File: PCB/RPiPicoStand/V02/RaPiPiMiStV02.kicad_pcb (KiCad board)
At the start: 4 copper layers, 55.5 x 73 mm, 27 parts, among them U1-PICO W Pico

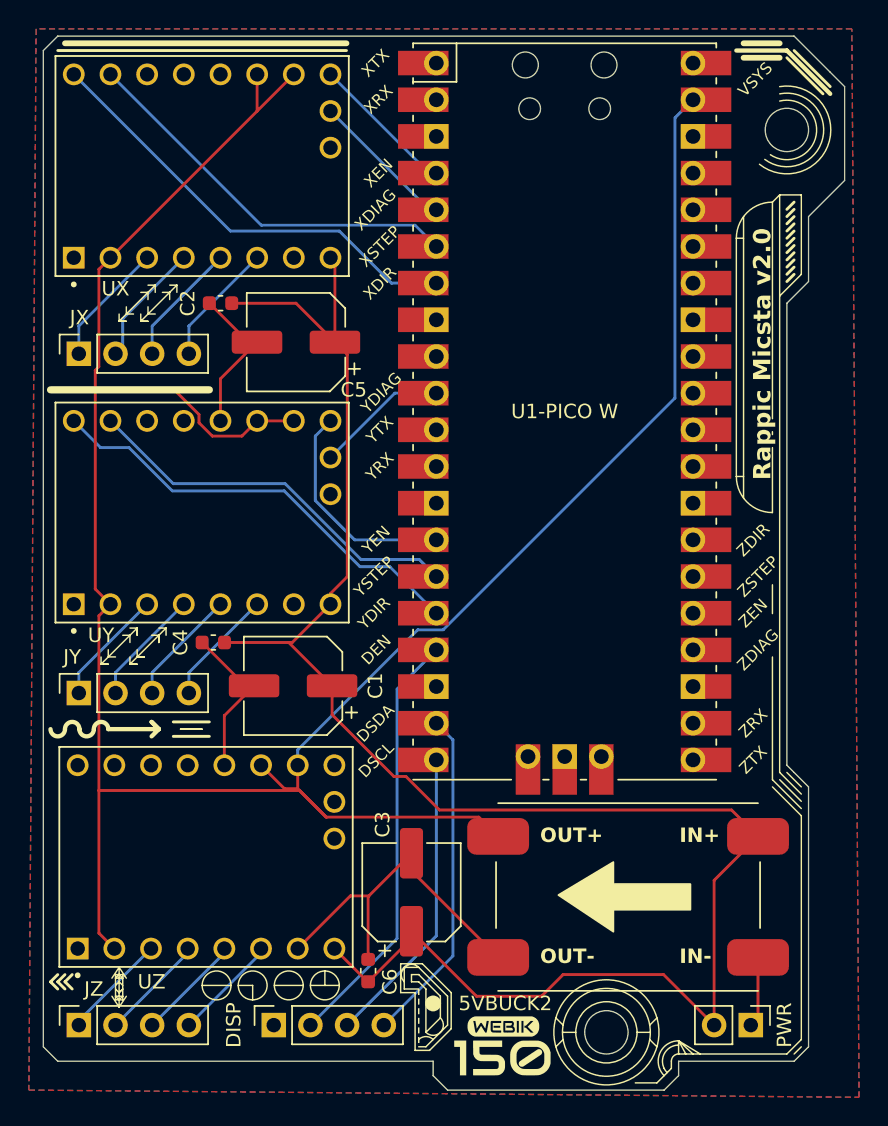
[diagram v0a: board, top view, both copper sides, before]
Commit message: fix uart connections on the PCB
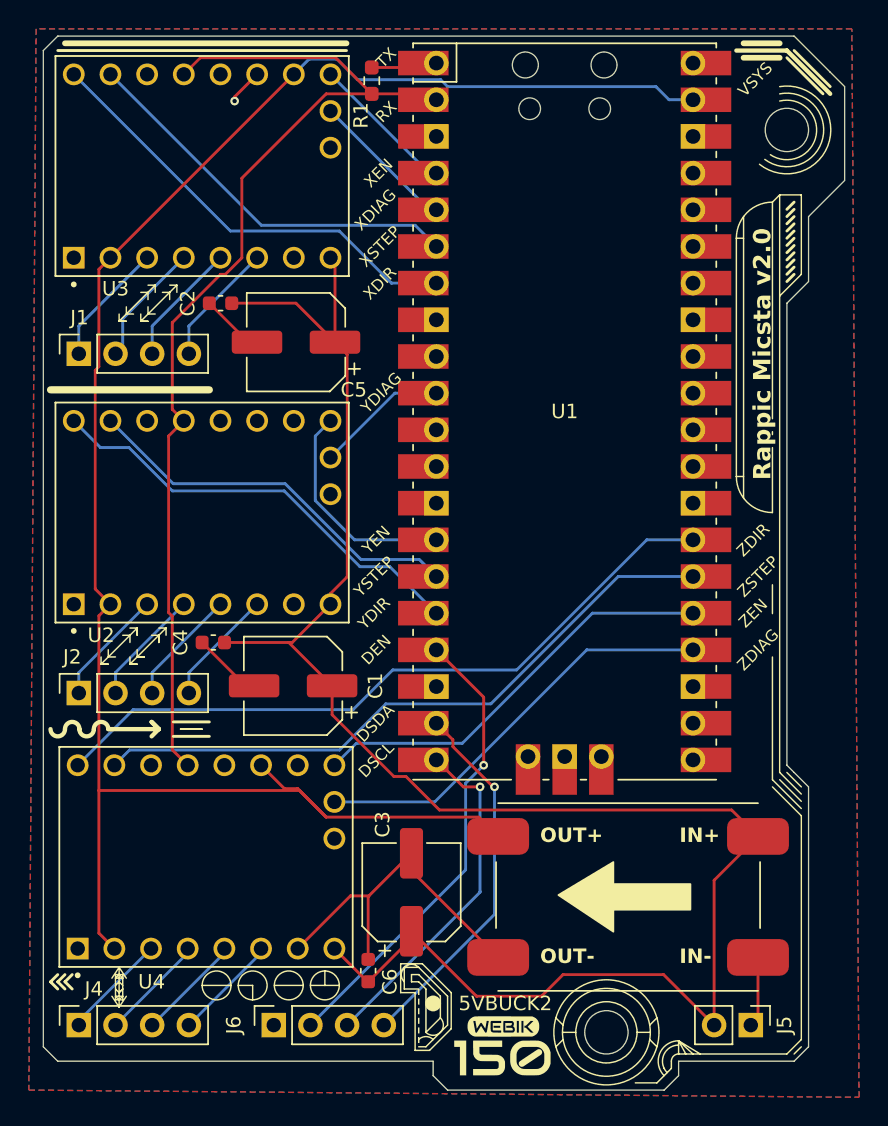
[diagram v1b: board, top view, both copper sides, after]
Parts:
- added R1: R_Small, Resistor_SMD:R_0603_1608Metric_Pad0.98x0.95mm_HandSolder, F.Cu at (170.2, 53.1)
- U1: renamed from U1-PICO W
- renumbered JX to J1, JY to J2, JZ to J4, PWR to J5, DISP to J6, UY to U2, UX to U3, UZ to U4
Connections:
- U1 pad 11: Net-(U1-GPIO8) -> unconnected-(U1-GPIO8-Pad11)
- U1 pad 12: Net-(U1-GPIO8) -> unconnected-(U1-GPIO9-Pad12)_1
- U1 pad 2: Net-(U1-GPIO0) -> Net-(U1-GPIO1)
- U1 pad 21: Net-(U1-GPIO16) -> unconnected-(U1-GPIO16-Pad21)
- U1 pad 22: Net-(U1-GPIO16) -> unconnected-(U1-GPIO17-Pad22)_1
- U2 pad 11: GND -> unconnected-(U2-PDN-Pad11)
- U2 pad 12: Net-(U1-GPIO8) -> Net-(U1-GPIO1)
- U2 pad 13: GND -> unconnected-(U2-SPRD-Pad13)
- U2 pad 14: Net-(5VBUCK2-OUT+) -> GND
- U2 pad 15: Net-(5VBUCK2-OUT+) -> GND
- U3 pad 11: GND -> unconnected-(U3-PDN-Pad11)
- U3 pad 12: Net-(U1-GPIO0) -> Net-(U1-GPIO1)
- U3 pad 13: GND -> unconnected-(U3-SPRD-Pad13)
- U3 pad 14: Net-(5VBUCK2-OUT+) -> GND
- U4 pad 11: GND -> unconnected-(U4-PDN-Pad11)
- U4 pad 12: Net-(U1-GPIO16) -> Net-(U1-GPIO1)
- U4 pad 13: GND -> unconnected-(U4-SPRD-Pad13)
- U4 pad 15: Net-(5VBUCK2-OUT+) -> GND
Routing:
- net Net-(U1-GPIO1): track 0.00 -> 74.8 mm
- net Net-(5VBUCK2-OUT+): track 180.9 -> 131.7 mm
- net Net-(U1-GPIO16): track 46.2 -> 0.00 mm
- net Net-(U1-GPIO8): track 24.7 -> 0.00 mm
- net Net-(U1-GPIO0): track 20.8 -> 4.60 mm
- net GND: track 51.7 -> 41.4 mm, vias 0 -> 1
- net Net-(J6-Pin_3): track 20.9 -> 24.1 mm, vias 0 -> 1
- net Net-(J6-Pin_2): track 29.6 -> 32.3 mm, vias 0 -> 1
- net Net-(J6-Pin_4): track 23.4 -> 25.8 mm, vias 0 -> 1
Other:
- copper layers 4 -> 2

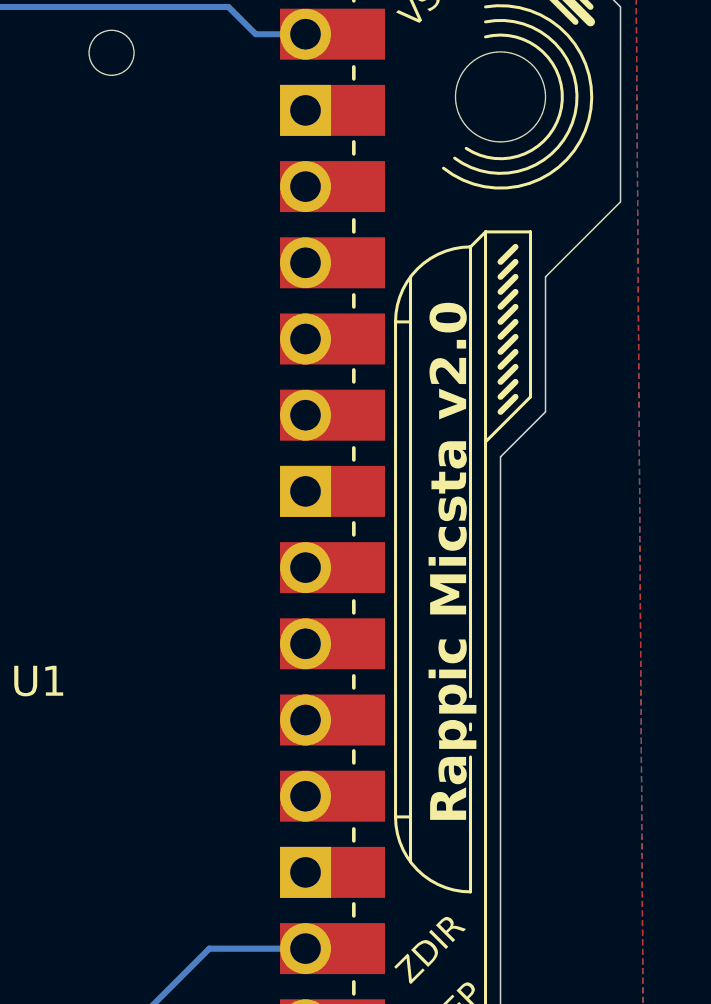
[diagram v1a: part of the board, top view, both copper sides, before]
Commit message: Update PCB design to V2.1 and adjust related files
Updated the PCB to version 2.1, introducing a simpler and cheaper 2-layer design compatible with more TMC2209 types. Adjusted KiCad project settings, output directories, and port configurations to align with the new PCB version. Updated README to document the changes.
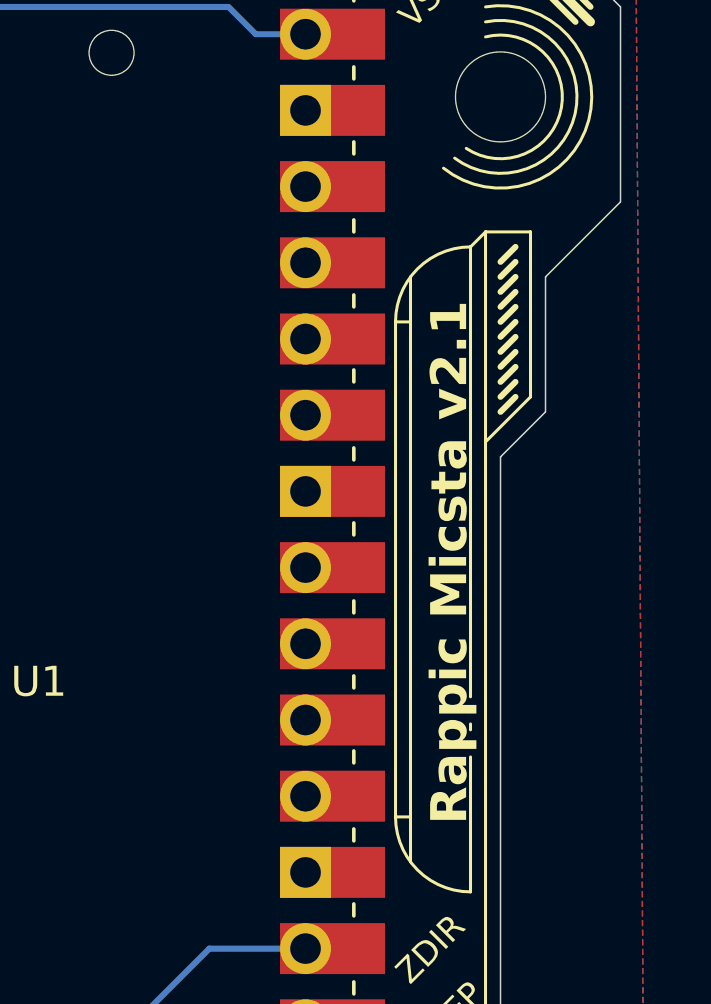
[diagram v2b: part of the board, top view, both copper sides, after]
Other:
- board text added: "Rappic Micsta v2.1"
- board text removed: "Rappic Micsta v2.0"
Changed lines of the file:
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@@
 			(drillshape 0)
 			(scaleselection 1)
-			(outputdirectory "")
+			(outputdirectory "factory-output/v21/")
 		)
 	)
@@
 		)
 		(fp_text user "TX"
-			(at -12.36 -24.5 225)
+			(at -12.36 -24.5 -135)
 			(layer "F.SilkS")
 			(effects
@@
 		)
 	)
-	(gr_text "Rappic Micsta v2.0"
+	(gr_text "Rappic Micsta v2.1"
 		(at 198 80.75 90)
 		(layer "F.SilkS")
@@
 			(justify left bottom)
 		)
-		(render_cache "Rappic Micsta v2.0" 90
+		(render_cache "Rappic Micsta v2.1" 90
 			(polygon
 				(pts
@@
 			(polygon
 				(pts
-					(xy 197.241871 63.337559) (xy 197.303158 63.342438) (xy 197.36281 63.350791) (xy 197.420444 63.3628)
-					(xy 197.50227 63.388063) (xy 197.577394 63.42257) (xy 197.644518 63.466931) (xy 197.702346 63.52176)
-					(xy 197.749581 63.587666) (xy 197.784925 63.665262) (xy 197.801243 63.723789) (xy 197.811315 63.787964)
-					(xy 197.814757 63.857969) (xy 197.81135 63.92799) (xy 197.801378 63.992212) (xy 197.785211 64.050811)
-					(xy 197.750163 64.128554) (xy 197.703273 64.194642) (xy 197.645798 64.24967) (xy 197.578994 64.294237)
-					(xy 197.504116 64.32894) (xy 197.422422 64.354374) (xy 197.364793 64.366476) (xy 197.305065 64.374902)
-					(xy 197.24361 64.379828) (xy 197.180801 64.38143) (xy 197.102098 64.378266) (xy 197.029547 64.369649)
-					(xy 196.962998 64.355903) (xy 196.902304 64.337352) (xy 196.821917 64.301226) (xy 196.753871 64.256113)
-					(xy 196.697664 64.203107) (xy 196.652798 64.143302) (xy 196.618773 64.077791) (xy 196.595087 64.00767)
-					(xy 196.581243 63.934031) (xy 196.57693 63.861193) (xy 196.857814 63.861193) (xy 196.858481 63.874703)
-					(xy 196.887371 63.939365) (xy 196.936949 63.974624) (xy 197.001123 63.996408) (xy 197.071845 64.007957)
-					(xy 197.141064 64.01251) (xy 197.200731 64.013307) (xy 197.27345 64.011778) (xy 197.338612 64.006676)
-					(xy 197.408434 63.994104) (xy 197.473463 63.967947) (xy 197.520653 63.918886) (xy 197.533976 63.857969)
-					(xy 197.533565 63.847239) (xy 197.508852 63.784636) (xy 197.46017 63.746937) (xy 197.402848 63.725456)
-					(xy 197.33243 63.711941) (xy 197.268008 63.706192) (xy 197.197507 63.704389) (xy 197.173406 63.704356)
-					(xy 197.106548 63.705307) (xy 197.03593 63.710958) (xy 196.96865 63.72534) (xy 196.911806 63.752485)
-					(xy 196.872495 63.796426) (xy 196.857814 63.861193) (xy 196.57693 63.861193) (xy 196.576739 63.857969)
-					(xy 196.582229 63.773168) (xy 196.598619 63.694213) (xy 196.625789 63.621649) (xy 196.663617 63.556021)
-					(xy 196.711985 63.497873) (xy 196.770772 63.447751) (xy 196.839857 63.4062) (xy 196.91912 63.373763)
-					(xy 196.977558 63.357472) (xy 197.04043 63.345636) (xy 197.107701 63.338416) (xy 197.179335 63.335973)
+					(xy 196.572636 63.621737) (xy 196.572636 63.90457) (xy 196.643853 63.923316) (xy 196.702352 63.950123)
+					(xy 196.759186 63.994523) (xy 196.799829 64.050492) (xy 196.826329 64.11746) (xy 196.838721 64.178571)
+					(xy 196.844417 64.246064) (xy 196.844918 64.2639) (xy 197.101959 64.2639) (xy 197.101959 63.98986)
+					(xy 197.796 63.98986) (xy 197.796 63.621737)
 				)
 			)
